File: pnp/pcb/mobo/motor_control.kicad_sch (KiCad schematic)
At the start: 0 parts

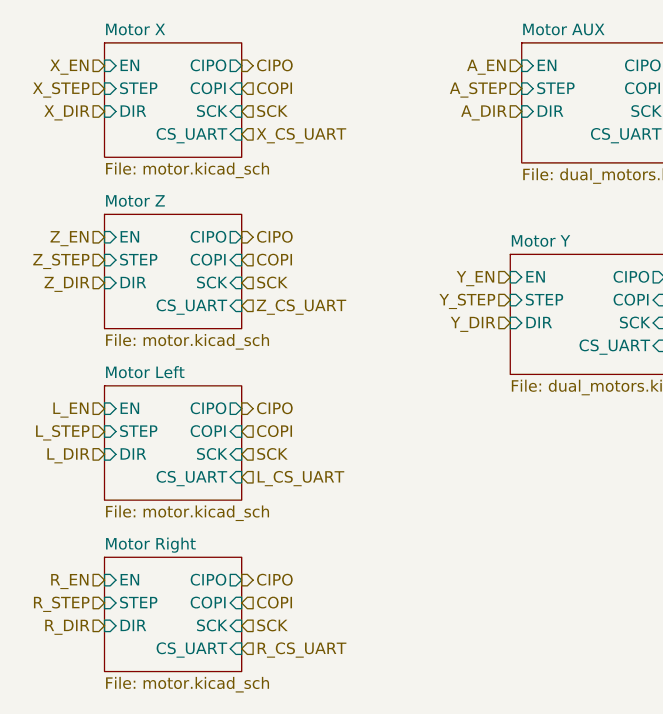
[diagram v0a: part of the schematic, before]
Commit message: Create a hierarchical structure
Put all circuits in to a single-function sheet
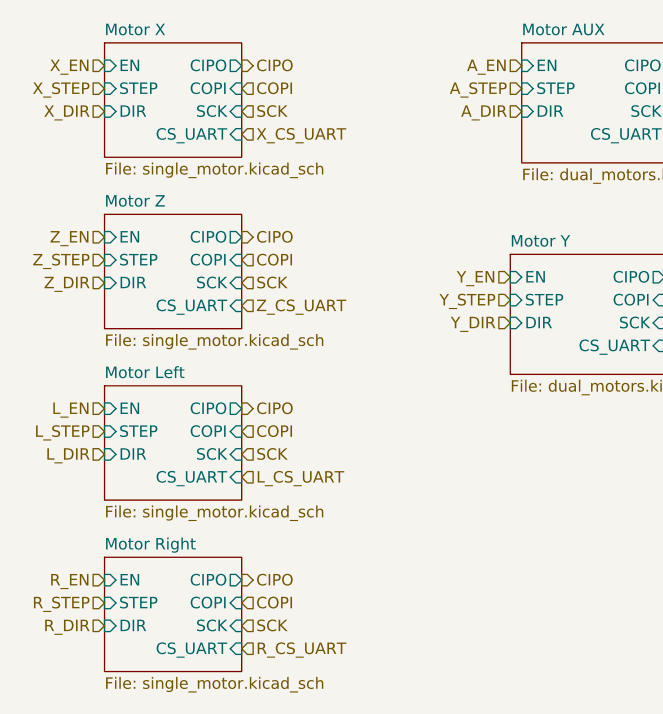
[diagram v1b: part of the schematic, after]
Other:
- sheet Motor Left: file motor.kicad_sch -> single_motor.kicad_sch
- sheet Motor Right: file motor.kicad_sch -> single_motor.kicad_sch
- sheet Motor X: file motor.kicad_sch -> single_motor.kicad_sch
- sheet Motor Z: file motor.kicad_sch -> single_motor.kicad_sch
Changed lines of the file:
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@@
       (effects (font (size 1.27 1.27)) (justify left bottom))
     )
-    (property "Sheet file" "motor.kicad_sch" (id 1) (at 119.38 83.7696 0)
+    (property "Sheet file" "single_motor.kicad_sch" (id 1) (at 119.38 83.7696 0)
       (effects (font (size 1.27 1.27)) (justify left top))
     )
@@
       (effects (font (size 1.27 1.27)) (justify left bottom))
     )
-    (property "Sheet file" "motor.kicad_sch" (id 1) (at 119.38 102.8196 0)
+    (property "Sheet file" "single_motor.kicad_sch" (id 1) (at 119.38 102.8196 0)
       (effects (font (size 1.27 1.27)) (justify left top))
     )
@@
       (effects (font (size 1.27 1.27)) (justify left bottom))
     )
-    (property "Sheet file" "motor.kicad_sch" (id 1) (at 119.38 121.8696 0)
+    (property "Sheet file" "single_motor.kicad_sch" (id 1) (at 119.38 121.8696 0)
       (effects (font (size 1.27 1.27)) (justify left top))
     )
@@
       (effects (font (size 1.27 1.27)) (justify left bottom))
     )
-    (property "Sheet file" "motor.kicad_sch" (id 1) (at 119.38 140.9196 0)
+    (property "Sheet file" "single_motor.kicad_sch" (id 1) (at 119.38 140.9196 0)
       (effects (font (size 1.27 1.27)) (justify left top))
     )

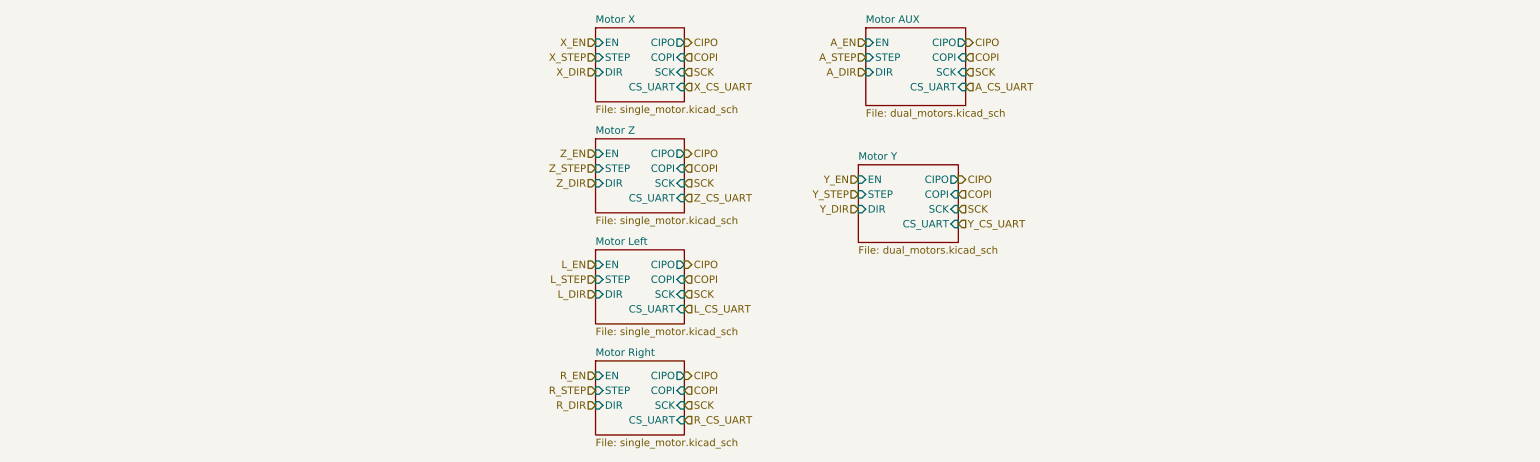
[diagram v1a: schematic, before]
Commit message: All sheets cleaned up
All symbols and their fields are now neatly organized.

All hierarchical pins are already imported,
except for the microcontroller sheet.
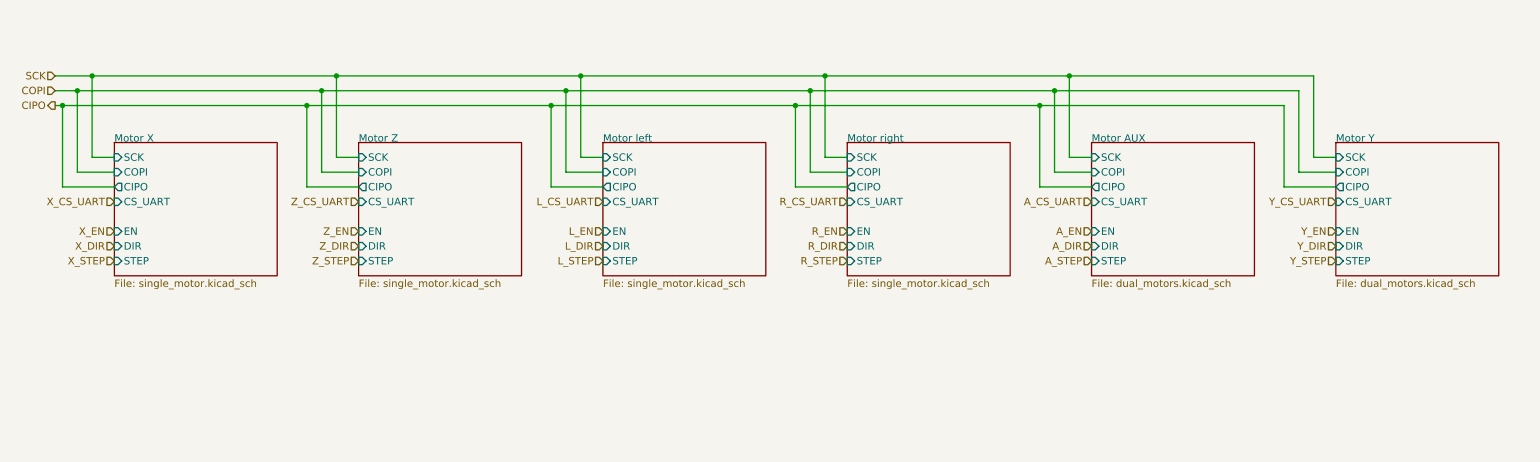
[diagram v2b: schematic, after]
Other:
- removed sheet Motor Left
- removed sheet Motor Right
- added sheet Motor left (single_motor.kicad_sch)
- added sheet Motor right (single_motor.kicad_sch)

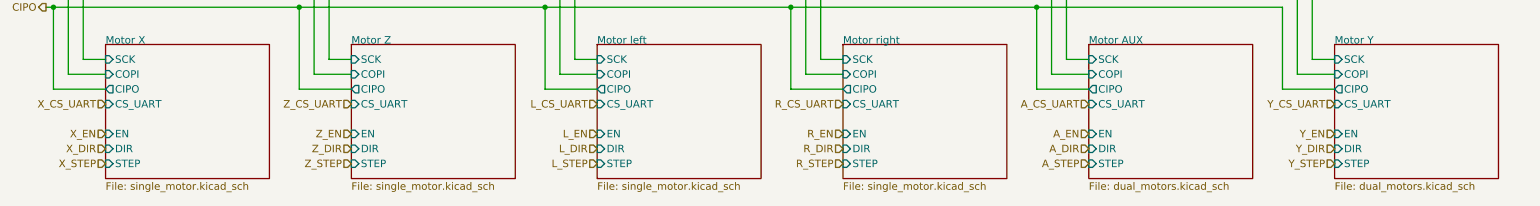
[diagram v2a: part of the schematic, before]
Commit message: Connect all sub-sheets together
Refactored schematic is checked against existing lay-out.
Connectivity has stayed the same.
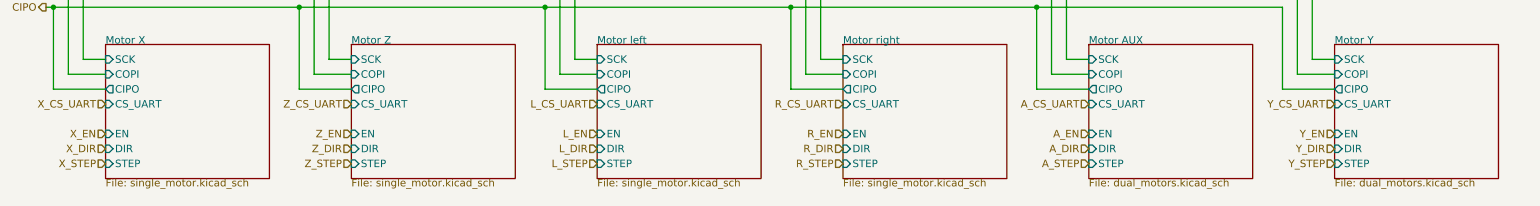
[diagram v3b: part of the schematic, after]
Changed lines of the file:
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@@
       (effects (font (size 1.27 1.27)) (justify left bottom))
     )
-    (property "Sheet file" "single_motor.kicad_sch" (id 1) (at 36.83 113.6146 0)
+    (property "Sheet file" "single_motor.kicad_sch" (id 1) (at 36.83 113.03 0)
       (effects (font (size 1.27 1.27)) (justify left top))
     )
@@
       (effects (font (size 1.27 1.27)) (justify left bottom))
     )
-    (property "Sheet file" "dual_motors.kicad_sch" (id 1) (at 204.47 113.6146 0)
+    (property "Sheet file" "dual_motors.kicad_sch" (id 1) (at 204.47 113.03 0)
       (effects (font (size 1.27 1.27)) (justify left top))
     )
@@
       (effects (font (size 1.27 1.27)) (justify left bottom))
     )
-    (property "Sheet file" "single_motor.kicad_sch" (id 1) (at 78.74 113.6146 0)
+    (property "Sheet file" "single_motor.kicad_sch" (id 1) (at 78.74 113.03 0)
       (effects (font (size 1.27 1.27)) (justify left top))
     )
@@
       (effects (font (size 1.27 1.27)) (justify left bottom))
     )
-    (property "Sheet file" "single_motor.kicad_sch" (id 1) (at 162.56 113.6146 0)
+    (property "Sheet file" "single_motor.kicad_sch" (id 1) (at 162.56 113.03 0)
       (effects (font (size 1.27 1.27)) (justify left top))
     )
@@
       (effects (font (size 1.27 1.27)) (justify left bottom))
     )
-    (property "Sheet file" "dual_motors.kicad_sch" (id 1) (at 246.38 113.6146 0)
+    (property "Sheet file" "dual_motors.kicad_sch" (id 1) (at 246.38 113.03 0)
       (effects (font (size 1.27 1.27)) (justify left top))
     )
@@
       (effects (font (size 1.27 1.27)) (justify left bottom))
     )
-    (property "Sheet file" "single_motor.kicad_sch" (id 1) (at 120.65 113.6146 0)
+    (property "Sheet file" "single_motor.kicad_sch" (id 1) (at 120.65 113.03 0)
       (effects (font (size 1.27 1.27)) (justify left top))
     )

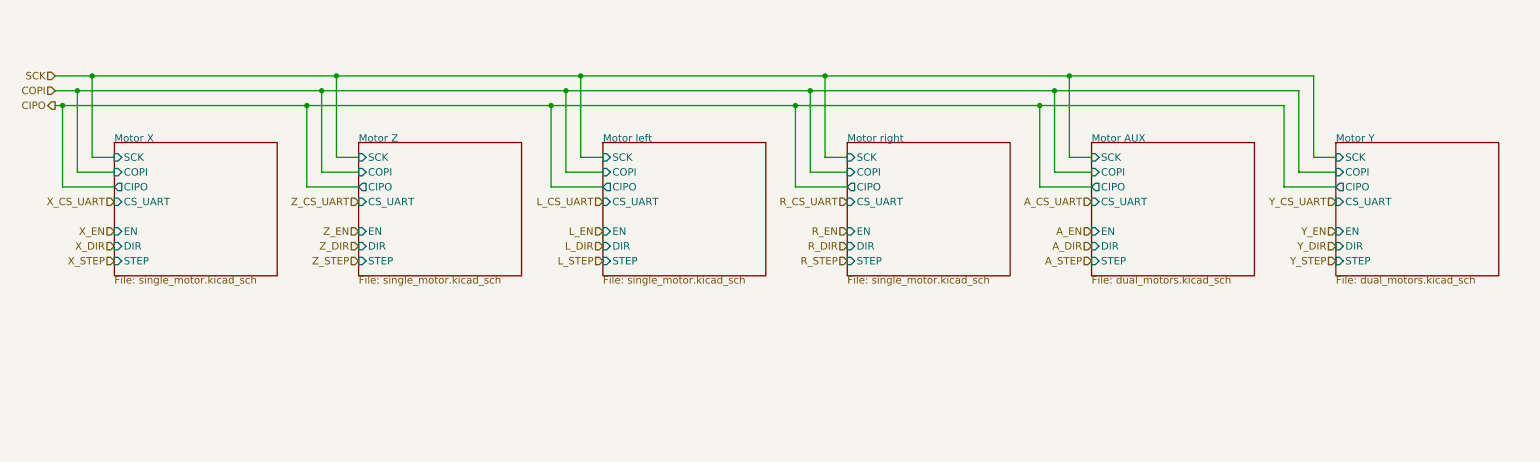
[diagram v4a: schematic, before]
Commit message: moving mobo-rev04b0 into mobo-rev04 branch from old repo
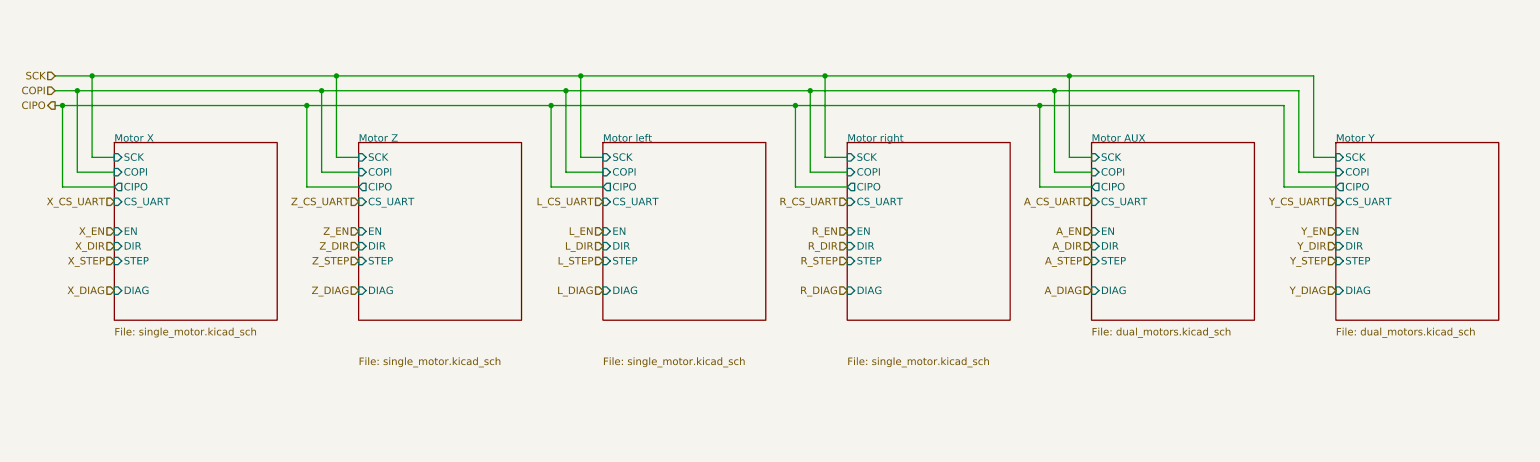
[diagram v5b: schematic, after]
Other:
- sheet Motor AUX ports: added DIAG; removed none
- sheet Motor X ports: added DIAG; removed none
- sheet Motor Y ports: added DIAG; removed none
- sheet Motor Z ports: added DIAG; removed none
- sheet Motor left ports: added DIAG; removed none
- sheet Motor right ports: added DIAG; removed none
- company: (none) -> Opulo
- title: Motors -> LumenPnP Motherboard
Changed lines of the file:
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@@
   (paper "A4")
   (title_block
-    (title "Motors")
+    (title "LumenPnP Motherboard")
     (date "2022-03-29")
     (rev "003")
+    (company "Opulo")
   )
   (junction (at 114.3 81.28) (diameter 0) (color 0 0 0 0)
@@
     (effects (font (size 1.27 1.27)) (justify right))
   )
+  (hierarchical_label "Z_DIAG" (shape input) (at 78.74 115.57 180)
+    (effects (font (size 1.27 1.27)) (justify right))
+  )
   (hierarchical_label "Z_CS_UART" (shape input) (at 78.74 100.33 180)
     (effects (font (size 1.27 1.27)) (justify right))
@@
     (effects (font (size 1.27 1.27)) (justify right))
   )
+  (hierarchical_label "A_DIAG" (shape input) (at 204.47 115.57 180)
+    (effects (font (size 1.27 1.27)) (justify right))
+  )
   (hierarchical_label "Z_STEP" (shape input) (at 78.74 110.49 180)
     (effects (font (size 1.27 1.27)) (justify right))
@@
     (effects (font (size 1.27 1.27)) (justify right))
   )
+  (hierarchical_label "L_DIAG" (shape input) (at 120.65 115.57 180)
+    (effects (font (size 1.27 1.27)) (justify right))
+  )
   (hierarchical_label "L_CS_UART" (shape input) (at 120.65 100.33 180)
     (effects (font (size 1.27 1.27)) (justify right))
@@
     (effects (font (size 1.27 1.27)) (justify right))
   )
+  (hierarchical_label "X_DIAG" (shape input) (at 36.83 115.57 180)
+    (effects (font (size 1.27 1.27)) (justify right))
+  )
   (hierarchical_label "R_EN" (shape input) (at 162.56 105.41 180)
     (effects (font (size 1.27 1.27)) (justify right))
   )
+  (hierarchical_label "Y_DIAG" (shape input) (at 246.38 115.57 180)
+    (effects (font (size 1.27 1.27)) (justify right))
+  )
   (hierarchical_label "R_CS_UART" (shape input) (at 162.56 100.33 180)
     (effects (font (size 1.27 1.27)) (justify right))
@@
     (effects (font (size 1.27 1.27)) (justify right))
   )
-  (sheet (at 36.83 90.17) (size 27.94 22.86)
+  (hierarchical_label "R_DIAG" (shape input) (at 162.56 115.57 180)
+    (effects (font (size 1.27 1.27)) (justify right))
+  )
+  (sheet (at 36.83 90.17) (size 27.94 30.48)
     (stroke (width 0) (type solid) (color 0 0 0 0))
     (fill (color 0 0 0 0.0000))
@@
       (effects (font (size 1.27 1.27)) (justify left bottom))
     )
-    (property "Sheet file" "single_motor.kicad_sch" (id 1) (at 36.83 113.03 0)
+    (property "Sheet file" "single_motor.kicad_sch" (id 1) (at 36.83 121.92 0)
       (effects (font (size 1.27 1.27)) (justify left top))
     )
@@
       (effects (font (size 1.27 1.27)) (justify left))
     )
-  )
-  (sheet (at 204.47 90.17) (size 27.94 22.86)
+    (pin "DIAG" input (at 36.83 115.57 180)
+      (effects (font (size 1.27 1.27)) (justify left))
+    )
+  )
+  (sheet (at 204.47 90.17) (size 27.94 30.48)
     (stroke (width 0) (type solid) (color 0 0 0 0))
     (fill (color 0 0 0 0.0000))
@@
       (effects (font (size 1.27 1.27)) (justify left bottom))
     )
-    (property "Sheet file" "dual_motors.kicad_sch" (id 1) (at 204.47 113.03 0)
+    (property "Sheet file" "dual_motors.kicad_sch" (id 1) (at 204.47 121.92 0)
       (effects (font (size 1.27 1.27)) (justify left top))
     )
@@
       (effects (font (size 1.27 1.27)) (justify left))
     )
-  )
-  (sheet (at 78.74 90.17) (size 27.94 22.86)
+    (pin "DIAG" input (at 204.47 115.57 180)
+      (effects (font (size 1.27 1.27)) (justify left))
+    )
+  )
+  (sheet (at 78.74 90.17) (size 27.94 30.48)
     (stroke (width 0) (type solid) (color 0 0 0 0))
     (fill (color 0 0 0 0.0000))
@@
       (effects (font (size 1.27 1.27)) (justify left bottom))
     )
-    (property "Sheet file" "single_motor.kicad_sch" (id 1) (at 78.74 113.03 0)
+    (property "Sheet file" "single_motor.kicad_sch" (id 1) (at 78.74 127 0)
       (effects (font (size 1.27 1.27)) (justify left top))
     )
@@
       (effects (font (size 1.27 1.27)) (justify left))
     )
-  )
-  (sheet (at 162.56 90.17) (size 27.94 22.86)
+    (pin "DIAG" input (at 78.74 115.57 180)
+      (effects (font (size 1.27 1.27)) (justify left))
+    )
+  )
+  (sheet (at 162.56 90.17) (size 27.94 30.48)
     (stroke (width 0) (type solid) (color 0 0 0 0))
     (fill (color 0 0 0 0.0000))
@@
       (effects (font (size 1.27 1.27)) (justify left bottom))
     )
-    (property "Sheet file" "single_motor.kicad_sch" (id 1) (at 162.56 113.03 0)
+    (property "Sheet file" "single_motor.kicad_sch" (id 1) (at 162.56 127 0)
       (effects (font (size 1.27 1.27)) (justify left top))
     )
@@
       (effects (font (size 1.27 1.27)) (justify left))
     )
-  )
-  (sheet (at 246.38 90.17) (size 27.94 22.86)
+    (pin "DIAG" input (at 162.56 115.57 180)
+      (effects (font (size 1.27 1.27)) (justify left))
+    )
+  )
+  (sheet (at 246.38 90.17) (size 27.94 30.48)
     (stroke (width 0) (type solid) (color 0 0 0 0))
     (fill (color 0 0 0 0.0000))
@@
       (effects (font (size 1.27 1.27)) (justify left bottom))
     )
-    (property "Sheet file" "dual_motors.kicad_sch" (id 1) (at 246.38 113.03 0)
+    (property "Sheet file" "dual_motors.kicad_sch" (id 1) (at 246.38 121.92 0)
       (effects (font (size 1.27 1.27)) (justify left top))
     )
@@
       (effects (font (size 1.27 1.27)) (justify left))
     )
-  )
-  (sheet (at 120.65 90.17) (size 27.94 22.86)
+    (pin "DIAG" input (at 246.38 115.57 180)
+      (effects (font (size 1.27 1.27)) (justify left))
+    )
+  )
+  (sheet (at 120.65 90.17) (size 27.94 30.48)
     (stroke (width 0) (type solid) (color 0 0 0 0))
     (fill (color 0 0 0 0.0000))
@@
       (effects (font (size 1.27 1.27)) (justify left bottom))
     )
-    (property "Sheet file" "single_motor.kicad_sch" (id 1) (at 120.65 113.03 0)
+    (property "Sheet file" "single_motor.kicad_sch" (id 1) (at 120.65 127 0)
       (effects (font (size 1.27 1.27)) (justify left top))
     )
@@
       (effects (font (size 1.27 1.27)) (justify left))
     )
+    (pin "DIAG" input (at 120.65 115.57 180)
+      (effects (font (size 1.27 1.27)) (justify left))
+    )
